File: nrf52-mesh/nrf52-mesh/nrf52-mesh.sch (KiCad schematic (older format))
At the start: 27 parts, among them J1 Conn_01x20_Male, J2 Conn_01x04_Male, J3 Conn_01x06_Male, U1 BL652

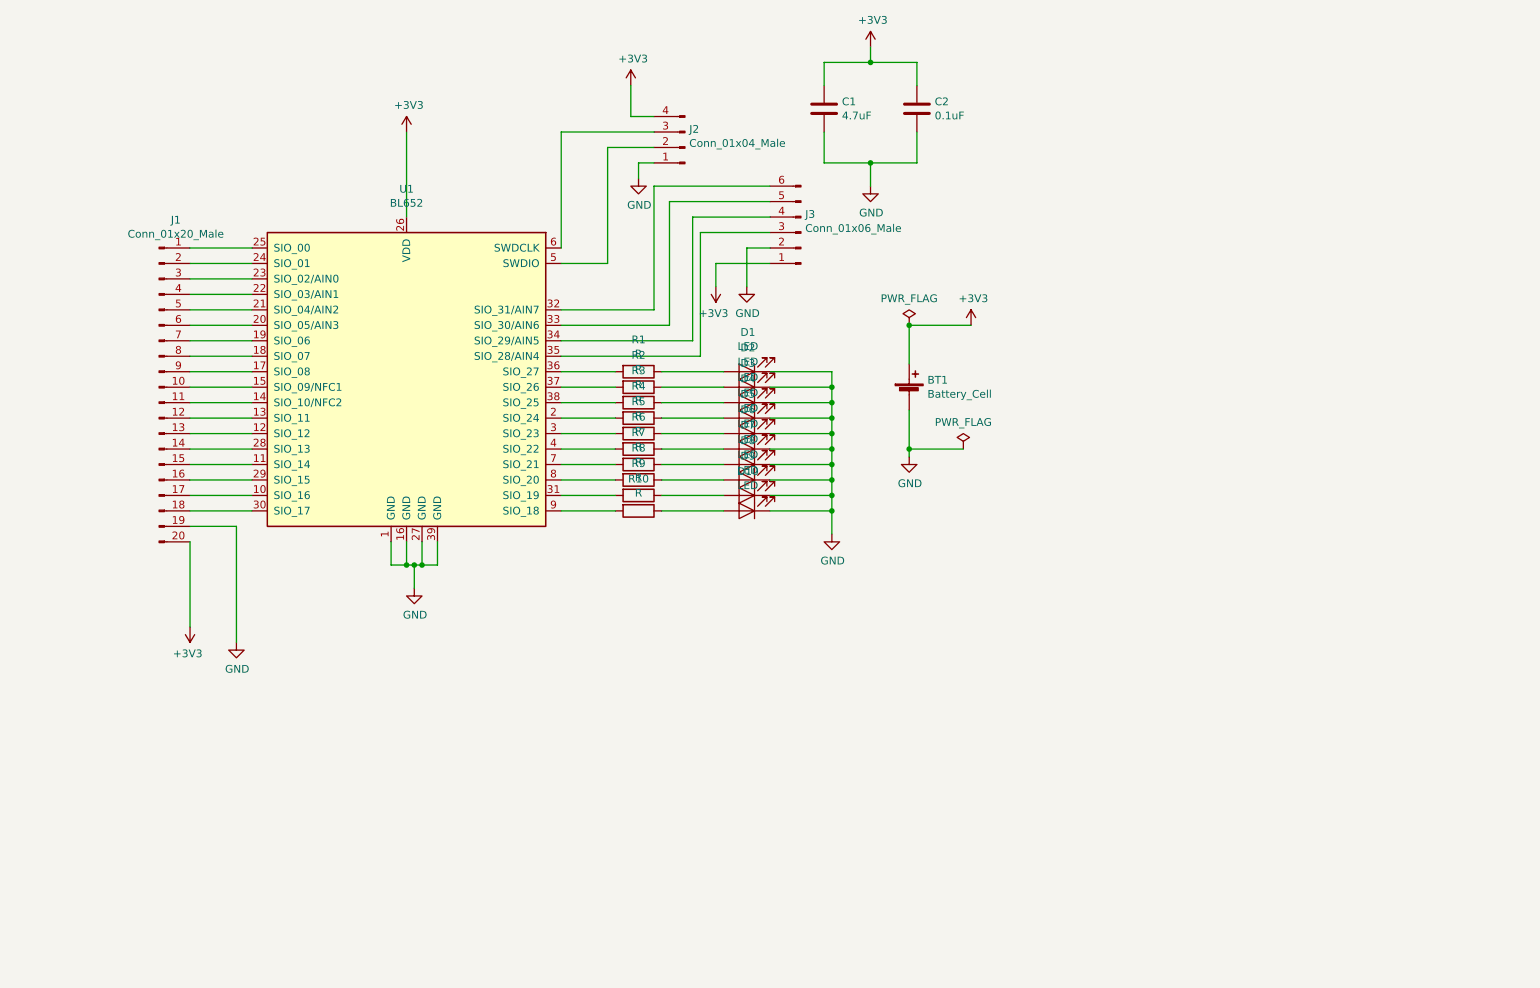
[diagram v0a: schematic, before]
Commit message: power for nrf52
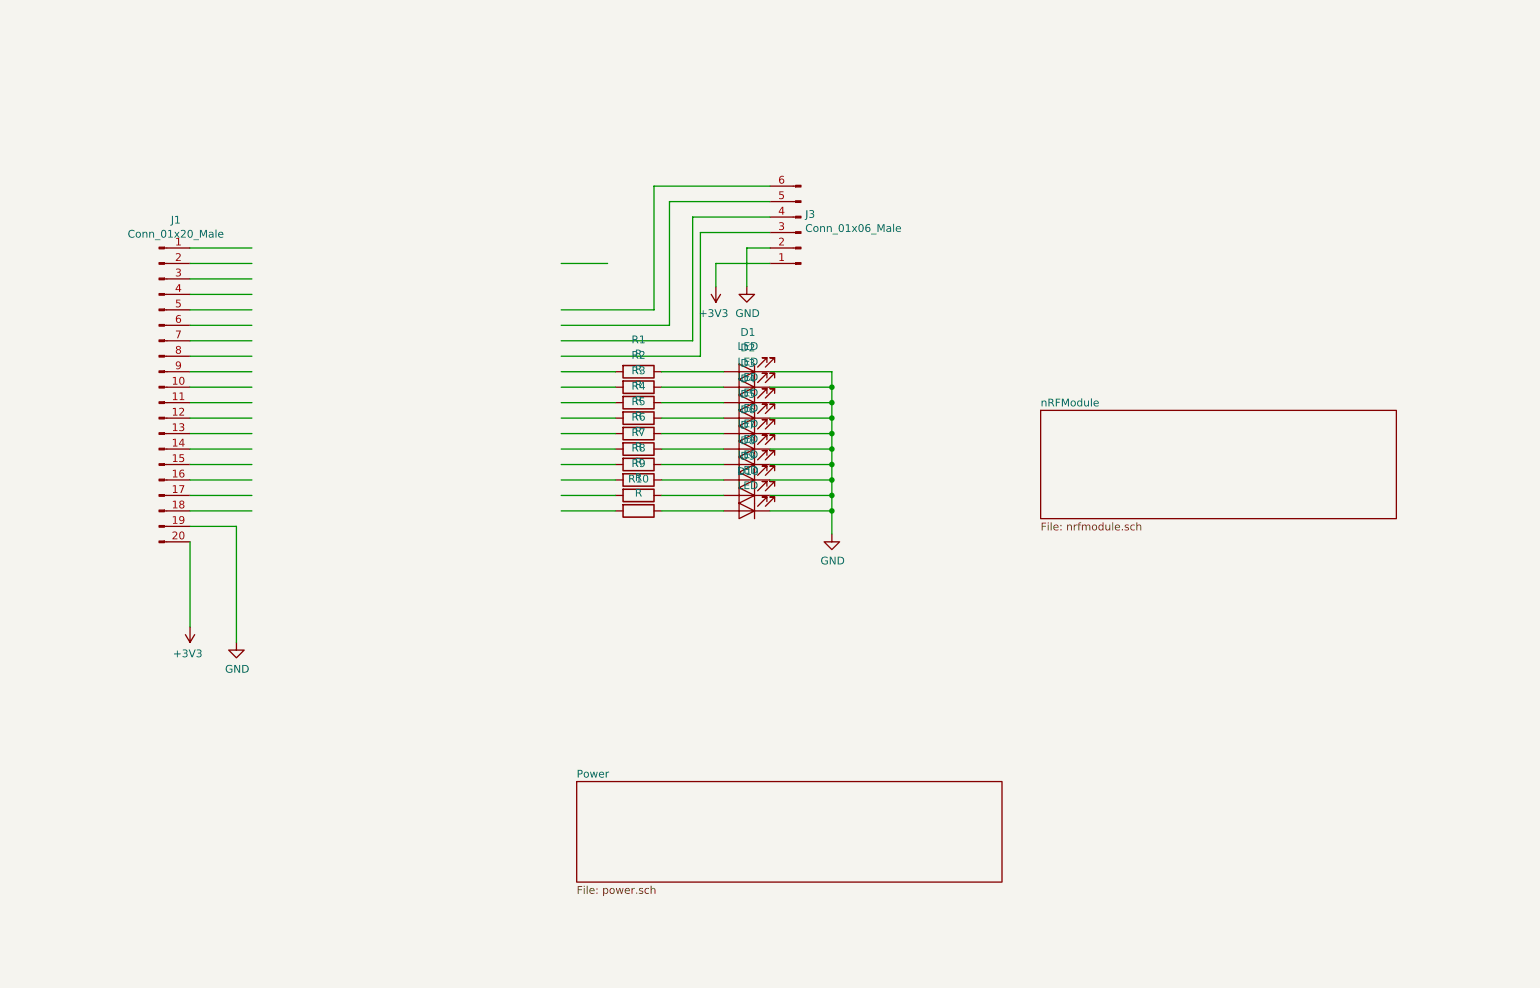
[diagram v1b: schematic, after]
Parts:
- removed BT1: Battery_Cell, kifootp:CR2032, symbol Device:Battery_Cell
- removed C1: 4.7uF, Capacitor_SMD:C_0402_1005Metric, symbol Device:C
- removed C2: 0.1uF, Capacitor_SMD:C_0402_1005Metric, symbol Device:C
- removed J2: Conn_01x04_Male, Connector_PinHeader_2.54mm:PinHeader_1x04_P2.54mm_Vertical, symbol Connector:Conn_01x04_Male
- removed U1: BL652, RF_Module:Laird_BL652, symbol RF_Bluetooth:BL652
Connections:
- wire segments 111 -> 78

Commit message: continue nRF52 power
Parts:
- removed D1, D10, D2, D3, D4, D5, D6, D7, D8, D9: LED, LED_SMD:LED_1206_3216Metric, symbol Device:LED
- removed J1: Conn_01x20_Male, Connector_PinHeader_2.54mm:PinHeader_1x20_P2.54mm_Vertical, symbol Connector:Conn_01x20_Male
- removed J3: Conn_01x06_Male, Connector_PinHeader_2.54mm:PinHeader_1x06_P2.54mm_Vertical, symbol Connector:Conn_01x06_Male
- removed R1, R2, R3, R4: R, Resistor_SMD:R_0402_1005Metric, symbol Device:R
- removed R10, R9: R, Resistor_SMD:R_1206_3216Metric, symbol Device:R
- removed R5, R6, R7, R8: R, Resistor_SMD:R_0805_2012Metric, symbol Device:R
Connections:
- net labels removed: +3V3, GND
- wire segments 78 -> 0

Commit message: next portion
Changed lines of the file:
@@
 $Descr A4 11693 8268
 encoding utf-8
-Sheet 1 7
+Sheet 1 8
 Title ""
 Date ""
@@
 F1 "io.sch" 50
 $EndSheet
+$Sheet
+S 2550 3450 2550 450
+U 5E55A119
+F0 "Debug" 50
+F1 "debug.sch" 50
+$EndSheet
 $EndSCHEMATC

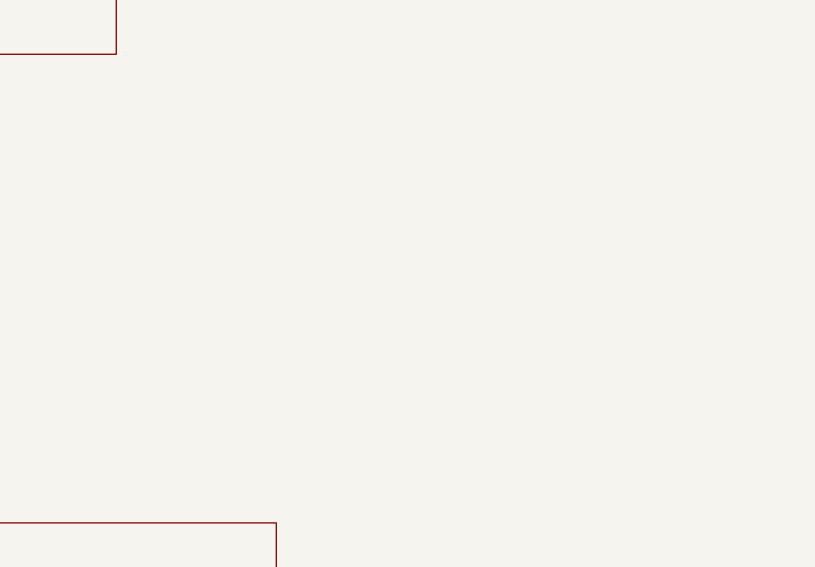
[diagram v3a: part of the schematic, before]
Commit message: nRF52 + ESP WROOM
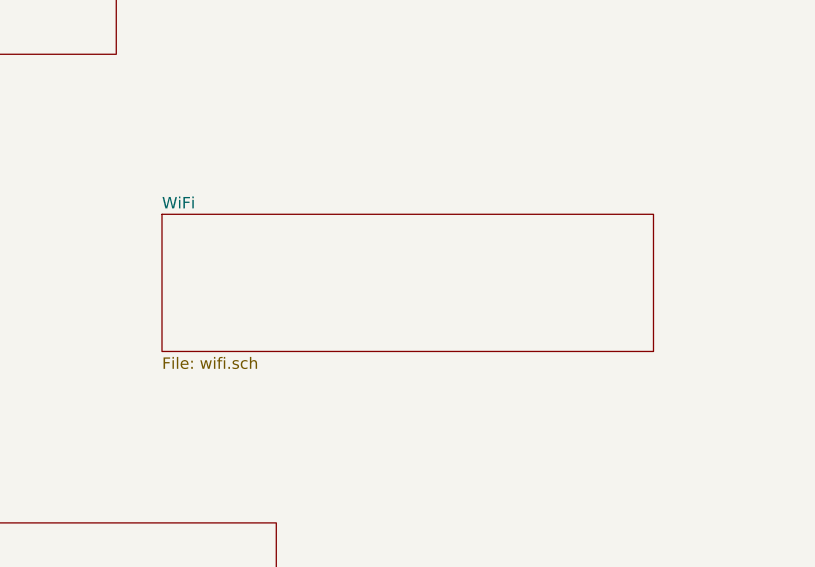
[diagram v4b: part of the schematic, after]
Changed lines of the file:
@@
 $Descr A4 11693 8268
 encoding utf-8
-Sheet 1 8
+Sheet 1 9
 Title ""
 Date ""
@@
 F1 "debug.sch" 50
 $EndSheet
+$Sheet
+S 4600 2100 2150 600
+U 5E8D2EF3
+F0 "WiFi" 50
+F1 "wifi.sch" 50
+$EndSheet
 $EndSCHEMATC
